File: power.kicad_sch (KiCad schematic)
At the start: 0 parts

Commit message: added main regulator parts
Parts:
- added U1: TPS53647RTAR, emberone:RTA0040B, symbol emberone:TPS53647RTAR
- added U2, U3, U4, U5: CSD95372BQ5M, emberone:DQP0012A, symbol emberone:CSD95372BQ5M

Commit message: pausing on the TPS53647 and trying the LM25119 for higher input voltage
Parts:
- added C1, C3: 270uF, symbol Device:C_Polarized
- added C10, C7, C8, C9: 47uF, symbol Device:C
- added C11: 1nF, symbol Device:C
- added C12, C13, C14, C15: 1uF, symbol Device:C
- added C2, C4, C5, C6: 22uF, symbol Device:C
- added R1: 4.32k, symbol Device:R_US
- added R10, R9: 150k, symbol Device:R_US
- added R11, R12: 24.3k, symbol Device:R_US
- added R13, R7, R8: 20k, symbol Device:R_US
- added R14: 121k, symbol Device:R_US
- added R15, R16: 1, symbol Device:R_US
- added R2: 22.1k, symbol Device:R_US
- added R3: 56.2k, symbol Device:R_US
- added R4: 9.31k, symbol Device:R_US
- added R5, R6: 16.5k, symbol Device:R_US
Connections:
- net at U1.1 (OCP-R): now also R1.2, R7.1
- net VSN: now reaches U1.10 (VSN)
- net at U1.14 (V3R3): now also C13.1
- net at U1.15 (V5): now also C15.1, R16.2
- net at U1.16 (V12): now also C14.1, R15.1
- net GND: now reaches U1.17 (GND)
- net GND: now also U1.20 (GND), U1.22 (GND), U1.41 (PAD), C11.2, C12.2, C15.2, R10.2, R11.2, R12.2, R13.2, R14.2, R7.2, R8.2, R9.2
- net VRRDY: now reaches U1.18 (VR_RDY)
- net VRHOT: now reaches U1.19 (VR_HOT_N)
- net at U1.21 (RESET_N): now also U1.23 (ENABLE), C12.1
- net SCL: now reaches U1.24 (PMB_CLK)
- net ALERT: now reaches U1.25 (PMB_ALERT_N)
- net SDA: now reaches U1.26 (PMB_DIO)
- net VRFAULT: now reaches U1.27 (VR_FAULT_N)
- net at U1.28 (ADDR_TRISE): now also R12.1, R6.2
- net at U1.29 (SLEW-MODE): now also R11.1, R5.2
- net CSP1: now reaches U1.3 (CSP1)
- net at U1.30 (O-USR): now also R10.1, R4.2
- net at U1.31 (VBOOT): now also R3.2, R9.1
- net at U1.32 (F-IMAX): now also R2.2, R8.1
- net SKIP: now reaches U1.39 (SKIP_NVM_N)
- net SKIP: now also R13.1
- net CSP2: now reaches U1.4 (CSP2)
- net TSEN: now reaches U1.40 (TSEN)
- net TSEN: now also C11.1, R14.1
- net CSP3: now reaches U1.5 (CSP3)
- net CSP4: now reaches U1.6 (CSP4)
- net VSP: now reaches U1.9 (VSP)
- new net: R1.1, R2.1, R3.1, R4.1, R5.1, R6.1
- new net PGND: C1.2, C10.2, C13.2, C14.2, C2.2, C3.2, C4.2, C5.2, C6.2, C7.2, C8.2, C9.2
- new net VIN: C1.1, C10.1, C2.1, C3.1, C4.1, C5.1, C6.1, C7.1, C8.1, C9.1, R15.2

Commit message: started adding LM25119
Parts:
- removed C11: 1nF, symbol Device:C
- removed C12, C13, C14, C15: 1uF, symbol Device:C
- removed C4: 22uF, symbol Device:C
- removed R10, R9: 150k, symbol Device:R_US
- removed R11, R12: 24.3k, symbol Device:R_US
- removed R13, R7, R8: 20k, symbol Device:R_US
- removed R14: 121k, symbol Device:R_US
- removed R15, R16: 1, symbol Device:R_US
- removed R4: 9.31k, symbol Device:R_US
- removed R5, R6: 16.5k, symbol Device:R_US
- removed U1: TPS53647RTAR, emberone:RTA0040B, symbol emberone:TPS53647RTAR
- removed U2, U3, U4, U5: CSD95372BQ5M, emberone:DQP0012A, symbol emberone:CSD95372BQ5M
- added C4: 82uF, symbol Device:C_Polarized
- added U1: LM25119PSQ/NOPB, emberone:SQA32A, symbol emberone:LM25119PSQ_NOPB
- C1, C3: value 270uF -> 82uF
- C10: value 47uF -> 820pF
- C2: value 22uF -> 0.1uF
- C5: value 22uF -> 1uF
- C6: value 22uF -> 820pF
- C7, C9: value 47uF -> 15nF
- C8: value 47uF -> 470nF
- R1: value 4.32k -> 56.2k
- R2: value 22.1k -> 9.09k
- R3: value 56.2k -> 44.2k
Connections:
- net PGND is gone; now on net GND: C1.2, C10.2, C2.2, C3.2, C5.2, C6.2, C7.2, C8.2, C9.2
- net GND: now also R2.2, R3.2, C4.2, U1.12 (AGND), U1.22 (PGND2), U1.33 (PAD)
- net VIN: now also R1.1, C4.1, U1.29 (VIN); no longer C10.1, C5.1, C6.1, C7.1, C8.1, C9.1
- net at R1.2: now also R2.1, U1.28 (UVLO)
- new net: C7.1, U1.18 (SS2)
- new net: C5.1, U1.1 (VCC1), U1.17 (DEMB)
- new net: C10.1, U1.6 (RAMP1)
- new net: C8.1, U1.14 (RES)
- new net: R3.1, U1.13 (RT)
- new net: C6.1, U1.19 (RAMP2)
- new net: C9.1, U1.7 (SS1)

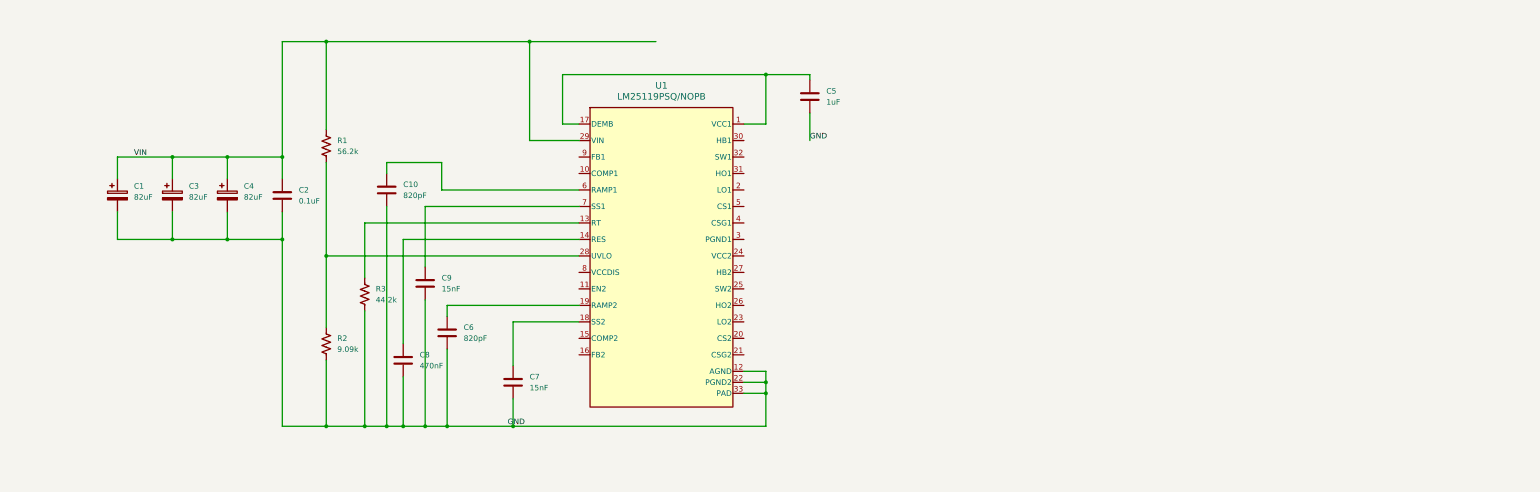
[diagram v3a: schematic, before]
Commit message: the voltage regulator schematic is in
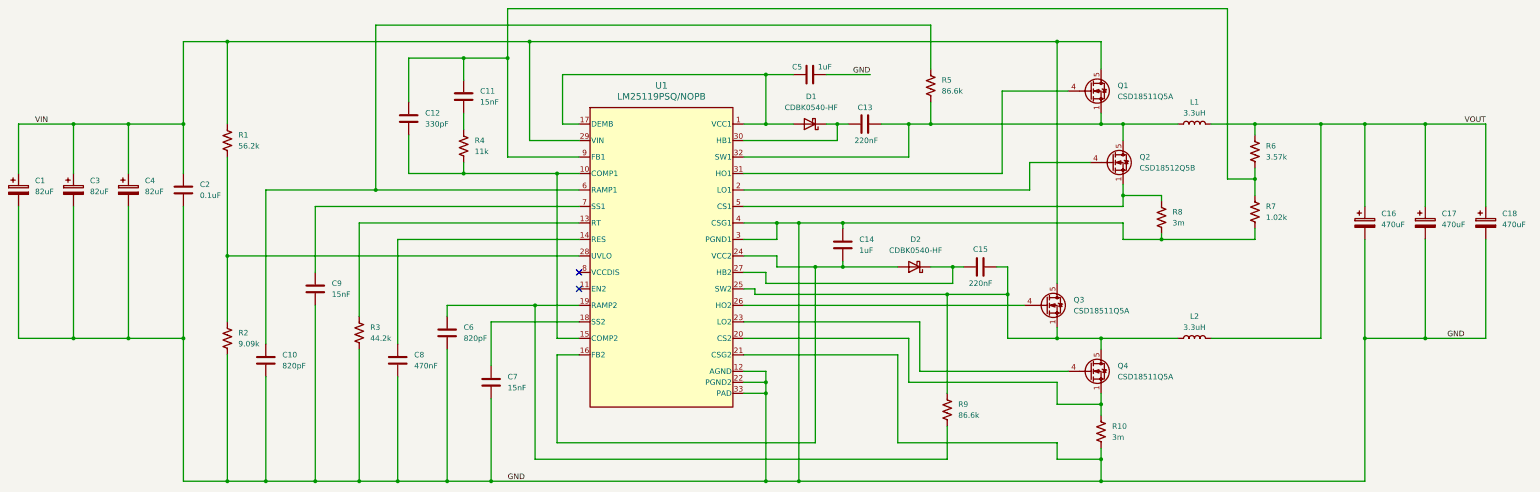
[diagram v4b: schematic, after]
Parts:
- added C11: 15nF, symbol Device:C
- added C12: 330pF, symbol Device:C
- added C13, C15: 220nF, symbol Device:C
- added C14: 1uF, symbol Device:C
- added C16, C17, C18: 470uF, symbol Device:C_Polarized
- added D1, D2: CDBK0540-HF, symbol Device:D_Schottky
- added L1, L2: 3.3uH, symbol Device:L
- added Q1, Q3, Q4: CSD18511Q5A, symbol Transistor_FET:CSD18501Q5A
- added Q2: CSD18512Q5B, symbol Transistor_FET:CSD18501Q5A
- added R10, R8: 3m, symbol Device:R_US
- added R4: 11k, symbol Device:R_US
- added R5, R9: 86.6k, symbol Device:R_US
- added R6: 3.57k, symbol Device:R_US
- added R7: 1.02k, symbol Device:R_US
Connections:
- net GND: now also U1.21 (CSG2), U1.3 (PGND1), U1.4 (CSG1), C14.1, C16.2, C17.2, C18.2, R10.2, R7.2, R8.2
- net VIN: now also Q1.5 (D), Q3.5 (D)
- net at C5.1, U1.1 (VCC1), U1.17 (DEMB): now also D1.2 (A)
- net at C10.1, U1.6 (RAMP1): now also R5.1
- net at U1.10 (COMP1): now also U1.15 (COMP2), C12.2, R4.2
- net at U1.16 (FB2): now also U1.24 (VCC2), C14.2, D2.2 (A)
- net at C6.1, U1.19 (RAMP2): now also R9.2
- net at U1.2 (LO1): now also Q2.4 (G)
- net at U1.20 (CS2): now also Q4.1 (S), Q4.2 (S), Q4.3 (S), R10.1
- net at U1.23 (LO2): now also Q4.4 (G)
- net at U1.25 (SW2): now also C15.2, L2.1, Q3.1 (S), Q3.2 (S), Q3.3 (S), Q4.5 (D), R9.1
- net at U1.26 (HO2): now also Q3.4 (G)
- net at U1.27 (HB2): now also C15.1, D2.1 (K)
- net at U1.30 (HB1): now also C13.1, D1.1 (K)
- net at U1.31 (HO1): now also Q1.4 (G)
- net at U1.32 (SW1): now also C13.2, L1.1, Q1.1 (S), Q1.2 (S), Q1.3 (S), Q2.5 (D), R5.2
- net at U1.5 (CS1): now also Q2.1 (S), Q2.2 (S), Q2.3 (S), R8.1
- net at U1.9 (FB1): now also C11.1, C12.1, R6.2, R7.1
- new net: C11.2, R4.1
- new net VOUT: C16.1, C17.1, C18.1, L1.2, L2.2, R6.1
- no-connect marks 0 -> 2
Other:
- moved on the sheet: C1, C10, C2, C3, C4, C5, C7, C8, C9, R1, R2, R3

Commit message: added all the power footprints, DS4432U and INA260 schematic
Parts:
- removed D2: CDBK0540-HF, symbol Device:D_Schottky
- removed Q1, Q3, Q4: CSD18511Q5A, symbol Transistor_FET:CSD18501Q5A
- removed Q2: CSD18512Q5B, symbol Transistor_FET:CSD18501Q5A
- added C19, C20: 1uF, Capacitor_SMD:C_0805_2012Metric, symbol Device:C
- added D2: XBS104S13R-G, emberone:SDO_4S13R-G_TOR, symbol Device:D_Filled
- added Q1, Q2, Q3, Q4: CSD18511Q5A, emberone:DQJ0008A, symbol emberone:CSD18511Q5A
- added R11: 80.6k, Resistor_SMD:R_0402_1005Metric, symbol Device:R_US
- added U2: DS4432U+, Package_SO:TSSOP-8_3x3mm_P0.65mm, symbol bitaxe:DS4432U+
- added U3: INA260, Package_SO:TSSOP-16_4.4x5mm_P0.65mm, symbol Sensor:INA260
- C1, C3, C4: footprint (none) -> emberone:PCAP_SVP_E12_PAN; DK (none) -> P16562CT-ND; Field6 (none) -> 35SVPF82M
- C10, C11, C12, C13, C14, C15, C2, C5, C6, C7, C8, C9: footprint (none) -> Capacitor_SMD:C_0805_2012Metric
- C16, C17, C18: footprint (none) -> emberone:CHEMI-H80; DK (none) -> 565-3164-1-ND; PARTNO (none) -> APXF6R3ARA471MH80G
- D1: value CDBK0540-HF -> XBS104S13R-G; footprint (none) -> emberone:SDO_4S13R-G_TOR; symbol Device:D_Schottky -> Device:D_Filled; DK (none) -> 893-1188-1-ND; PARTNO (none) -> XBS104S13R-G
- L1, L2: footprint (none) -> emberone:IND_SER2915L_COC; DK (none) -> 2457-SER2915L-332KL-ND; PARTNO (none) -> SER2915L-332KL
- R1, R2, R3, R4, R6, R7, R9: footprint (none) -> Resistor_SMD:R_0603_1608Metric
- R10, R8: footprint (none) -> emberone:WSR-4527; DK (none) -> WSRA-.003CT-ND; PARTNO (none) -> WSR23L000FEA
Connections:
- net GND: now also C19.2, C20.2, R11.2, U2.4 (GND), U3.11 (GND), U3.4 (A1), U3.5 (A0), U3.6 (GND)
- net VIN: now also U3.1 (IN+), U3.12 (VBUS), U3.2 (IN+), U3.3 (IN+); no longer C1.1, C2.1, C3.1, C4.1, R1.1, U1.29 (VIN)
- net at C15.1, U1.27 (HB2): now also D2.1 (K)
- net at C15.2, L2.1, R9.1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: now also Q3.1 (S), Q3.2 (S), Q3.3 (S), Q4.5 (D), Q4.6 (D), Q4.7 (D), Q4.8 (D)
- net at U1.26 (HO2): now also Q3.4 (G)
- net at R10.1, U1.20 (CS2): now also Q4.1 (S), Q4.2 (S), Q4.3 (S)
- net at U1.23 (LO2): now also Q4.4 (G)
- net at C13.2, L1.1, R5.2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: now also Q1.1 (S), Q1.2 (S), Q1.3 (S), Q2.5 (D), Q2.6 (D), Q2.7 (D), Q2.8 (D)
- net at C14.2, U1.16 (FB2), U1.24 (VCC2): now also D2.2 (A)
- net OUT0: now reaches C11.1, C12.1, R6.2, R7.1, U1.9 (FB1)
- net OUT0: now also U2.6 (OUT0)
- net at R8.1, U1.5 (CS1): now also Q2.1 (S), Q2.2 (S), Q2.3 (S)
- net at U1.2 (LO1): now also Q2.4 (G)
- net at U1.31 (HO1): now also Q1.4 (G)
- new net: R11.1, U2.5 (FS0)
- new net 3V3: C19.1, C20.1, U2.8 (VCC), U3.10 (VS)
- new net SCL: U2.2 (SCL), U3.9 (SCL)
- new net SDA: U2.1 (SDA), U3.8 (SDA)
- new net VIN_M: C1.1, C2.1, C3.1, C4.1, Q1.5 (D), Q1.6 (D), Q1.7 (D), Q1.8 (D), Q3.5 (D), Q3.6 (D), Q3.7 (D), Q3.8 (D), R1.1, U1.29 (VIN), U3.14 (IN-), U3.15 (IN-), U3.16 (IN-)
- no-connect marks 2 -> 4
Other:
- note added: "DS4432U+ Lets us change the LM25119 voltage over I2C"
- note added: "I2C Address: 0x40"
- note added: "I2C Address: 0x48"
- note added: "LM25119PSQ/NOPB 11V-25V to 3.60V @ 40A https://webench.ti.com/appinfo/webench/scripts/SDP.cgi?ID=B73486FF40F315FE"
- note added: "Power Monitor"
- moved on the sheet: C1, C10, C11, C12, C13, C14, C15, C16, C2, C5, C6, C7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

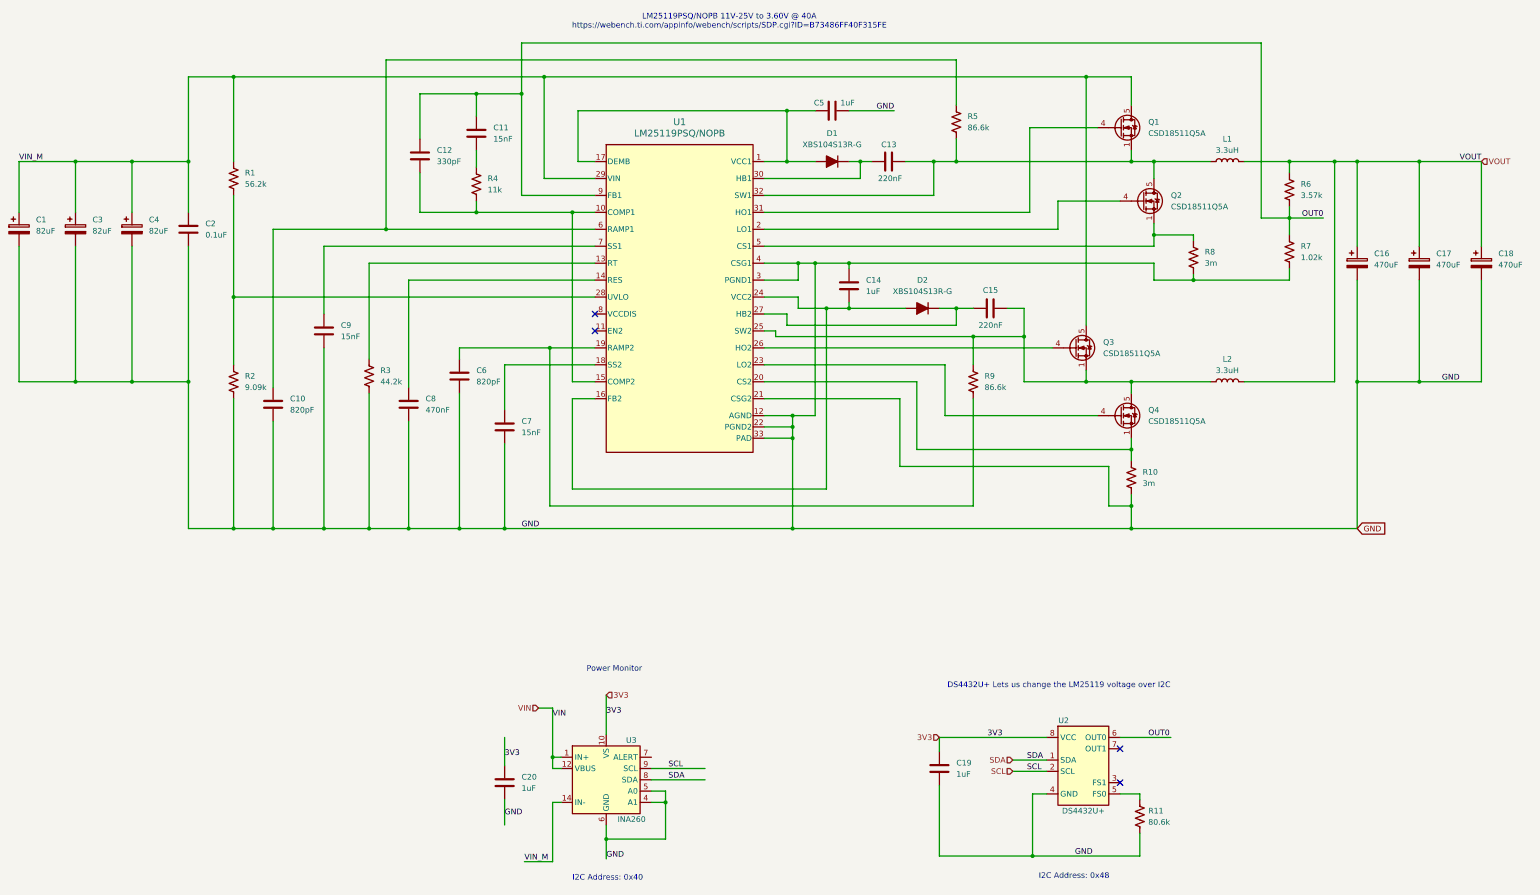
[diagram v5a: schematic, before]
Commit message: schematic done, started initial placement
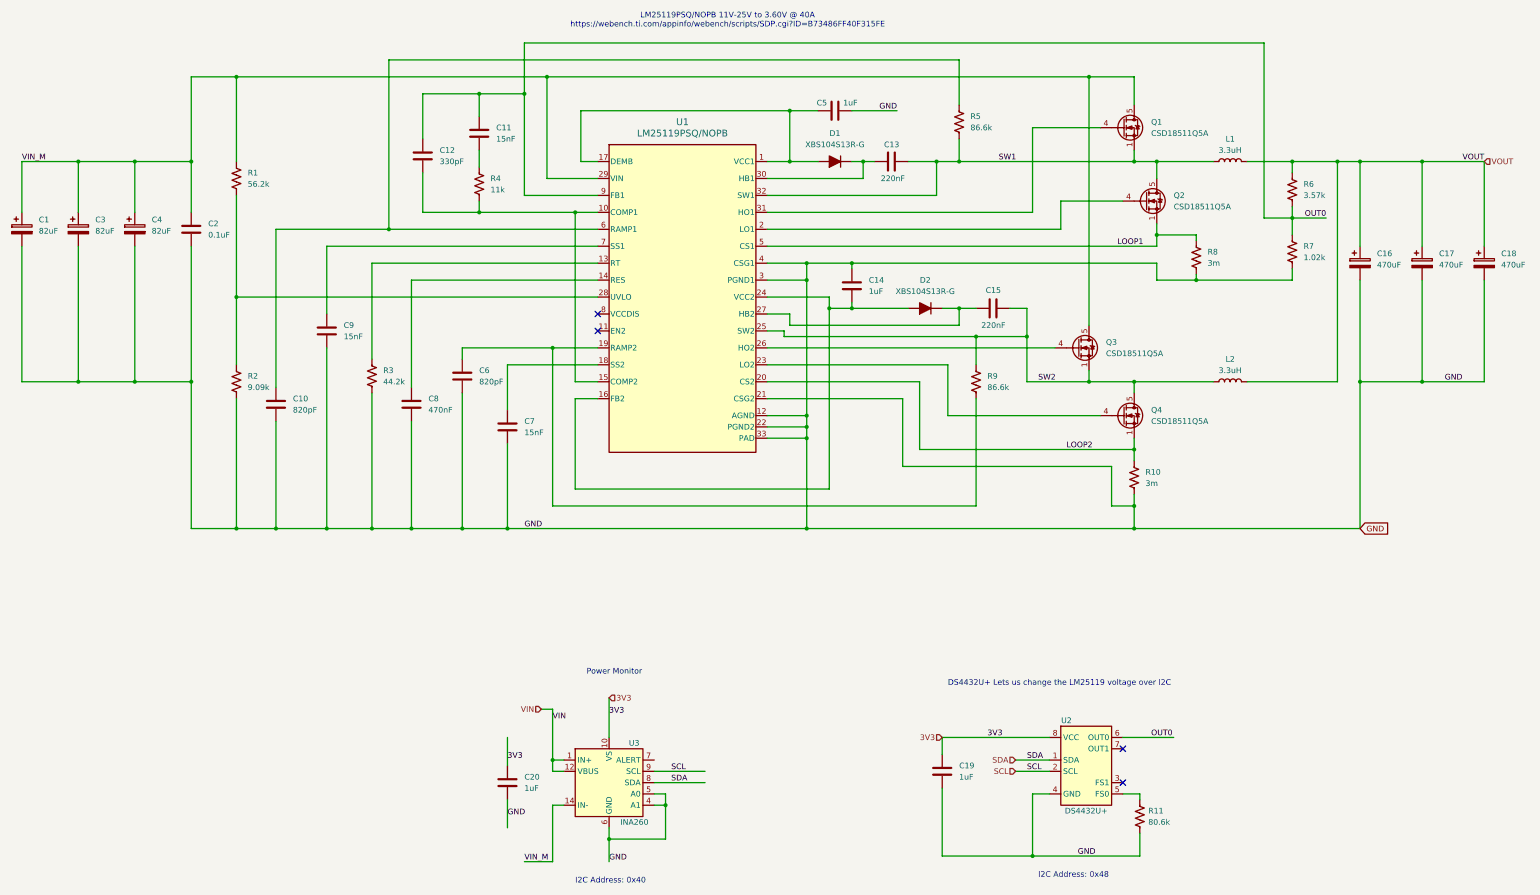
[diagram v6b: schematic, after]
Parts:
- R5: footprint (none) -> Resistor_SMD:R_0603_1608Metric
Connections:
- net SW2: now reaches C15.2, L2.1, Q3.1 (S), Q3.2 (S), Q3.3 (S), Q4.5 (D), Q4.6 (D), Q4.7 (D), Q4.8 (D), R9.1, U1.25 (SW2)
- net LOOP1: now reaches Q2.1 (S), Q2.2 (S), Q2.3 (S), R8.1, U1.5 (CS1)
- net LOOP2: now reaches Q4.1 (S), Q4.2 (S), Q4.3 (S), R10.1, U1.20 (CS2)
- net SW1: now reaches C13.2, L1.1, Q1.1 (S), Q1.2 (S), Q1.3 (S), Q2.5 (D), Q2.6 (D), Q2.7 (D), Q2.8 (D), R5.2, U1.32 (SW1)
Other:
- moved on the sheet: C1, C10, C11, C12, C13, C14, C15, C16, C17, C18, C19, C2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

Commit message: finished routing. passes DRC
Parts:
- added H1, H2, H3, H4: MountingHole, MountingHole:MountingHole_3.5mm, symbol Mechanical:MountingHole
- L1, L2: symbol Device:L -> emberone:L

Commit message: added schematic partnumbers
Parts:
- C10, C6: DK (none) -> 311-1194-1-ND; PARTNO (none) -> CC0805KRX7R9BB821
- C11, C7, C9: value 15nF -> 0.015uF; DK (none) -> 399-C0805C153K5RAC7800CT-ND; PARTNO (none) -> C0805C153K5RAC7800
- C12: DK (none) -> 399-C0805C331J5GAC7800CT-ND; PARTNO (none) -> C0805C331J5GAC7800
- C13, C15: value 220nF -> 0.22uF; DK (none) -> 1276-2947-1-ND; PARTNO (none) -> CL21B224KBFNFNE
- C14, C19, C20, C5: DK (none) -> 1276-6470-1-ND; PARTNO (none) -> CL21B105KBFNNNG
- C2: DK (none) -> 311-1140-1-ND; PARTNO (none) -> CC0805KRX7R9BB104
- C8: value 470nF -> 0.47uF; DK (none) -> 1276-6482-1-ND; PARTNO (none) -> CL21B474KBFNNNG
- R1: DK (none) -> 311-56.2KHRCT-ND; PARTNO (none) -> RC0603FR-0756K2L
- R2: DK (none) -> 311-9.09KHRCT-ND; PARTNO (none) -> RC0603FR-079K09L
- R3: DK (none) -> 311-44.2KHRCT-ND; PARTNO (none) -> RC0603FR-0744K2L
- R4: DK (none) -> 311-11.0KHRCT-ND; PARTNO (none) -> RC0603FR-0711KL
- R5, R9: DK (none) -> 311-86.6KHRCT-ND; PARTNO (none) -> RC0603FR-0786K6L
- R6: DK (none) -> 311-3.57KHRCT-ND; PARTNO (none) -> RC0603FR-073K57L
- R7: DK (none) -> 311-1.02KHRCT-ND; PARTNO (none) -> RC0603FR-071K02L
